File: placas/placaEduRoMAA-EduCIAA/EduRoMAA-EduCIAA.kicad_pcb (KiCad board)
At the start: 2 copper layers, 103 x 80 mm, 78 parts, among them J1 DC_IN, J2 Motor_Izq, J3 Motor_Der, J4 Bluetooth, J5 Sonar, J6 DC_OUT, J7 DC_IN, Q1 BC548, Q2 BC548, Q3 BC548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

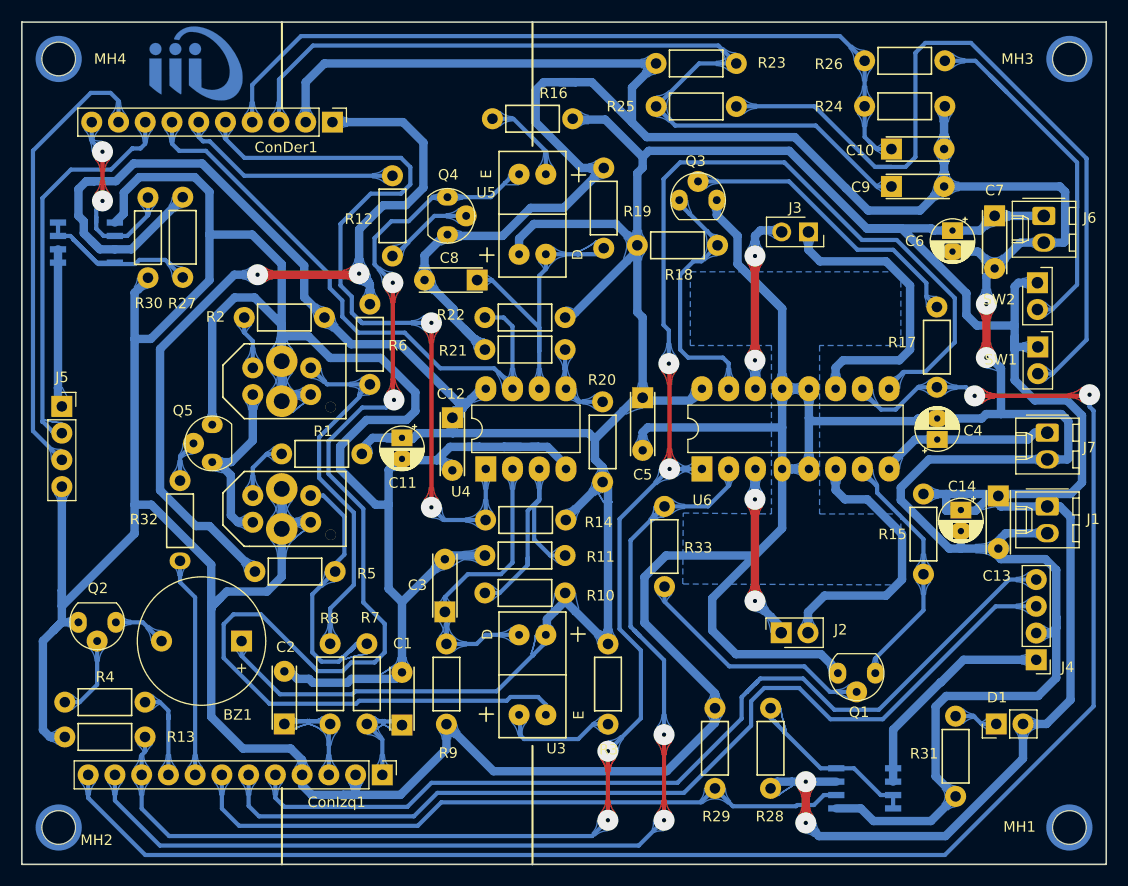
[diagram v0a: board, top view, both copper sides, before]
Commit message: [PCB] Modifico serigrafia y re-ruteo.
Modifico serigrafia y algo de ruteo
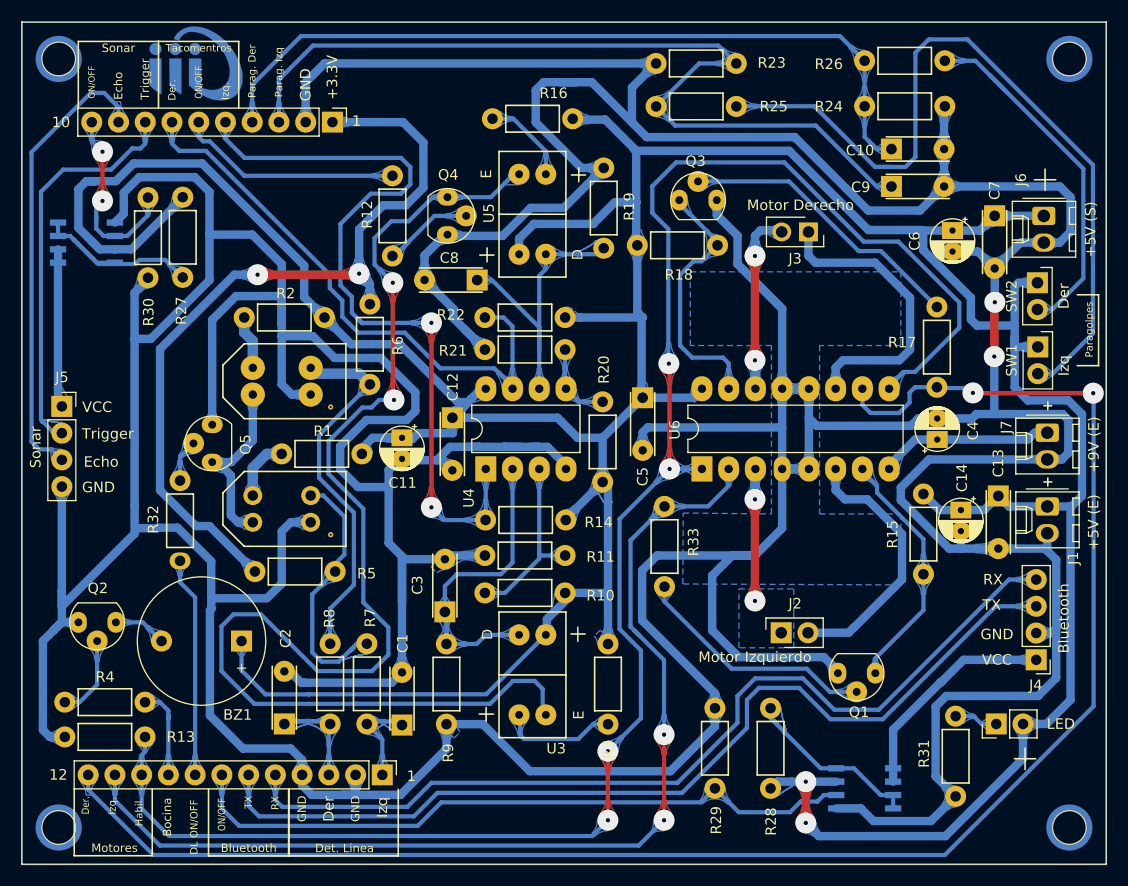
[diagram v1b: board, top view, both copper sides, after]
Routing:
- net +5V: track 416.8 -> 398.9 mm
- net GND: track 777.5 -> 766.9 mm
- net PWM_Der: track 168.8 -> 161.9 mm
- net Net-(R10-Pad2): track 23.9 -> 17.5 mm
- net GND_LED2: track 118.5 -> 122.1 mm
- net /Motor_Izq1: track 16.6 -> 13.1 mm
- net Bluetooth_Rx: track 89.2 -> 87.8 mm
- net /Motor_Izq2: track 26.5 -> 25.4 mm
- net ENABLE_Motors: track 169.4 -> 170.3 mm
- net Net-(R25-Pad2): track 75.5 -> 76.3 mm
- net Net-(Q3-Pad2): track 28.4 -> 27.6 mm
- net Net-(C3-Pad1): track 28.4 -> 29.1 mm
- net Sonar_Trig: track 37.5 -> 38.0 mm
- added copper zone on B.Cu, net /Motor_Izq1
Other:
- board text added: "+3.3V"
- board text added: "+5V (E)"
- board text added: "+5V (S)"
- board text added: "+9V (E)"
- board text added: "1"
- board text added: "10"
- board text added: "12"
- board text added: "Bluetooth"
- board text added: "Bocina"
- board text added: "DL ON/OFF"
- board text added: "Der"
- board text added: "Der."
- board text added: "Det. Linea"
- board text added: "Echo"
- board text added: "GND"
- board text added: "Habil."
- board text added: "Izq"
- board text added: "Izq."
- board text added: "LED"
- board text added: "Motor Derecho"
- board text added: "Motor Izquierdo"
- board text added: "Motores"
- board text added: "ON/OFF"
- board text added: "Parag. Der"
- board text added: "Parag. Izq"
- board text added: "Paragolpes"
- board text added: "RX"
- board text added: "Sonar"
- board text added: "TX"
- board text added: "Tacomentros"
- board text added: "Trigger"
- board text added: "VCC"

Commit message: [PCB] Revisiones de ruteado.
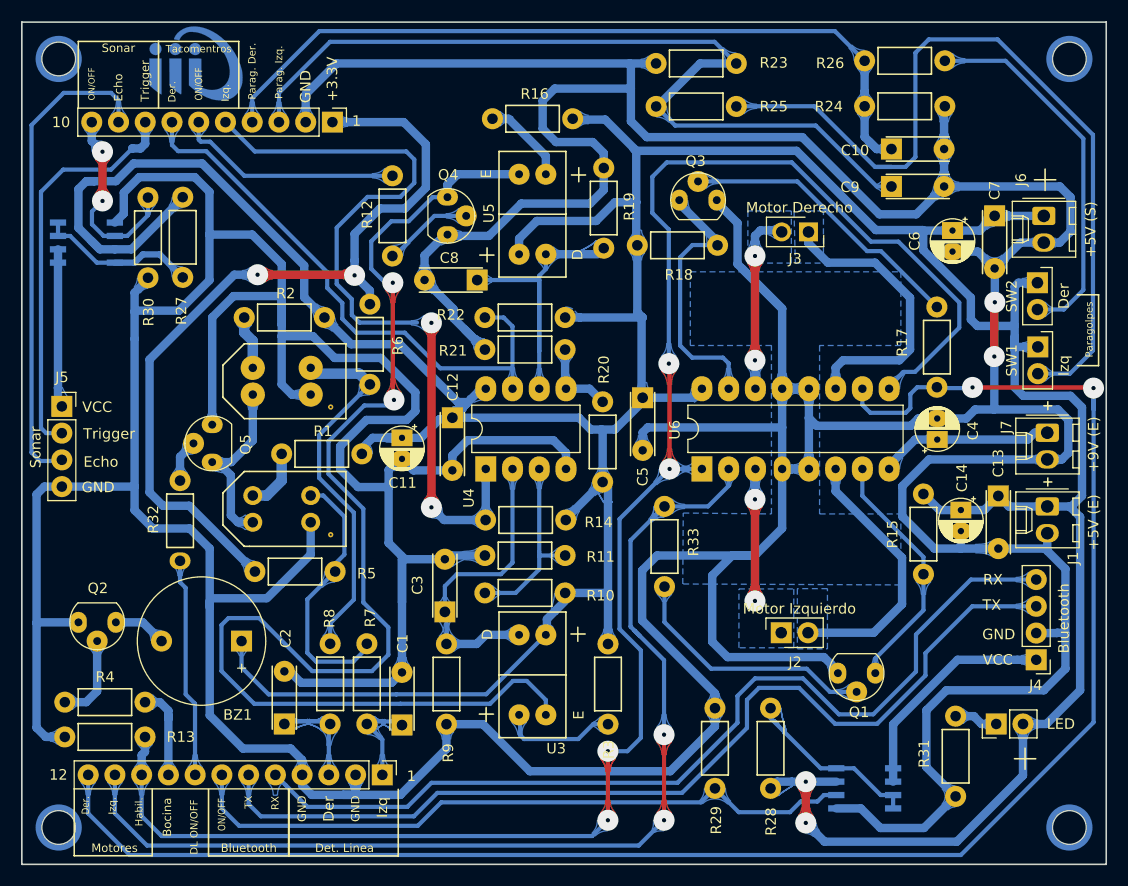
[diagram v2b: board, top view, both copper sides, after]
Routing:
- net GND: track 766.9 -> 760.6 mm
- net Net-(R27-Pad2): track 20.0 -> 15.4 mm
- net Encoder_Izq: track 78.4 -> 74.2 mm
- net PWM_Der: track 161.9 -> 165.7 mm
- net Net-(C8-Pad1): track 28.8 -> 31.4 mm
- net Net-(R25-Pad2): track 76.3 -> 78.9 mm
- net Sonar_Echo: track 43.7 -> 46.3 mm
- net ENABLE_Motors: track 170.3 -> 172.3 mm
- net Bluetooth_Tx: track 90.5 -> 92.0 mm
- net +5V: track 398.9 -> 400.3 mm
- net Net-(Q1-Pad2): track 23.2 -> 24.4 mm
- net Net-(D1-Pad1): track 5.18 -> 4.15 mm
- net Bluetooth_Rx: track 87.8 -> 88.9 mm
- net /C_2: track 25.1 -> 26.1 mm
- net Net-(R5-Pad2): track 23.7 -> 24.6 mm
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- added copper zone on B.Cu, net /Motor_Der1
- added copper zone on B.Cu, net /Motor_Der2
- added copper zone on B.Cu, net /Motor_Izq2
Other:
- board text added: "Parag. Der."
- board text added: "Parag. Izq."
- board text removed: "Parag. Der"
- board text removed: "Parag. Izq"

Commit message: [PCB] Agrego serigrafia complementaria
Agrego símbolos para serigrafia, lista para revision
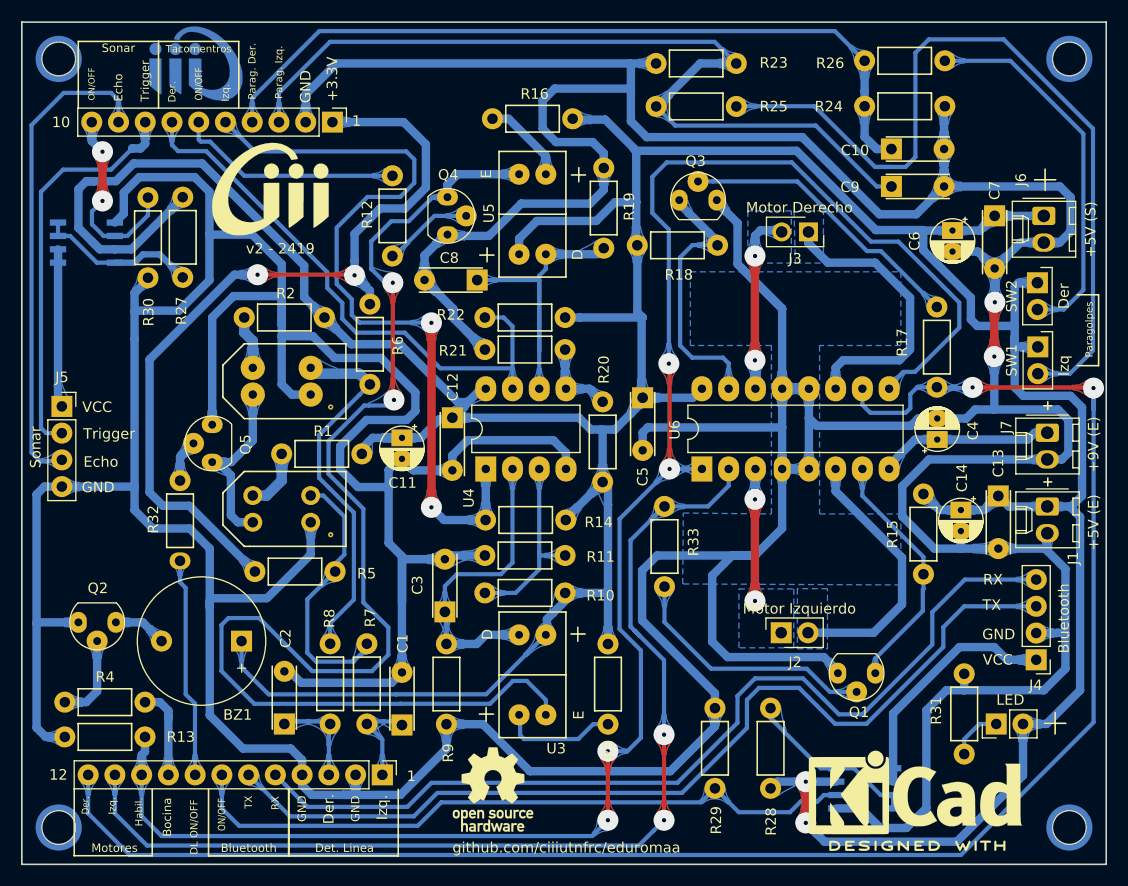
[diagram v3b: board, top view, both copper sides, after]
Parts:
- added Logo_2: Logo_CIII, lib_fp:Logo_CIII_Small_FSilk, F.Cu at (89.6, 70.9)
- added Logo_3: Logo_ohw, lib_fp:OSHW-Logo_7.5x8mm_SilkScreen, F.Cu at (110.7, 127.9)
- added Logo_4: Logo_KiCad, lib_fp:KiCad-Logo2_8mm_SilkScreen, F.Cu at (150.9, 128.1)
- moved R31 11.7 mm to (155.5, 116.9), turned to 270 degrees
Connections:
- net +3.3VA renamed +3V3
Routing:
- net /Vcc_BT: track 21.6 -> 25.0 mm
- net Bluetooth_Tx: track 92.0 -> 90.2 mm
- net GND: track 760.6 -> 758.9 mm
- net Encoder_Izq: track 74.2 -> 75.5 mm
- net Net-(D1-Pad1): track 4.15 -> 5.05 mm
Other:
- net class Default: clearance 0.5 -> 0.2
- net class power: clearance 0.5 -> 0.2
- rule trace_clearance: 0.5 -> 0.2
- board text added: "github.com/ciiiutnfrc/eduromaa"
- board text added: "v2 - 2419"

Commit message: [PCB] Arreglo teardrops
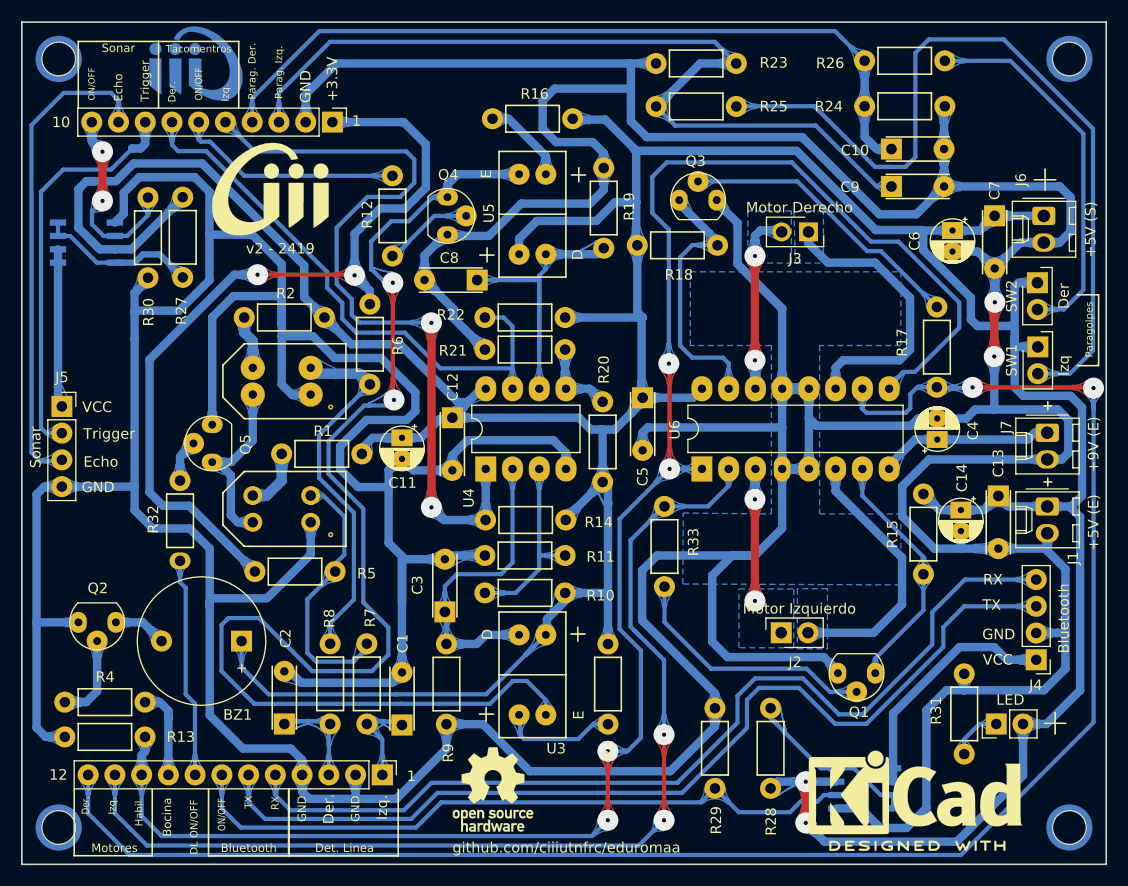
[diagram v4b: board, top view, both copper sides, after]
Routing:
- net Bluetooth_Tx: track 90.2 -> 91.9 mm
- net Bluetooth_Rx: track 88.6 -> 90.0 mm
- net GND: track 758.9 -> 757.9 mm

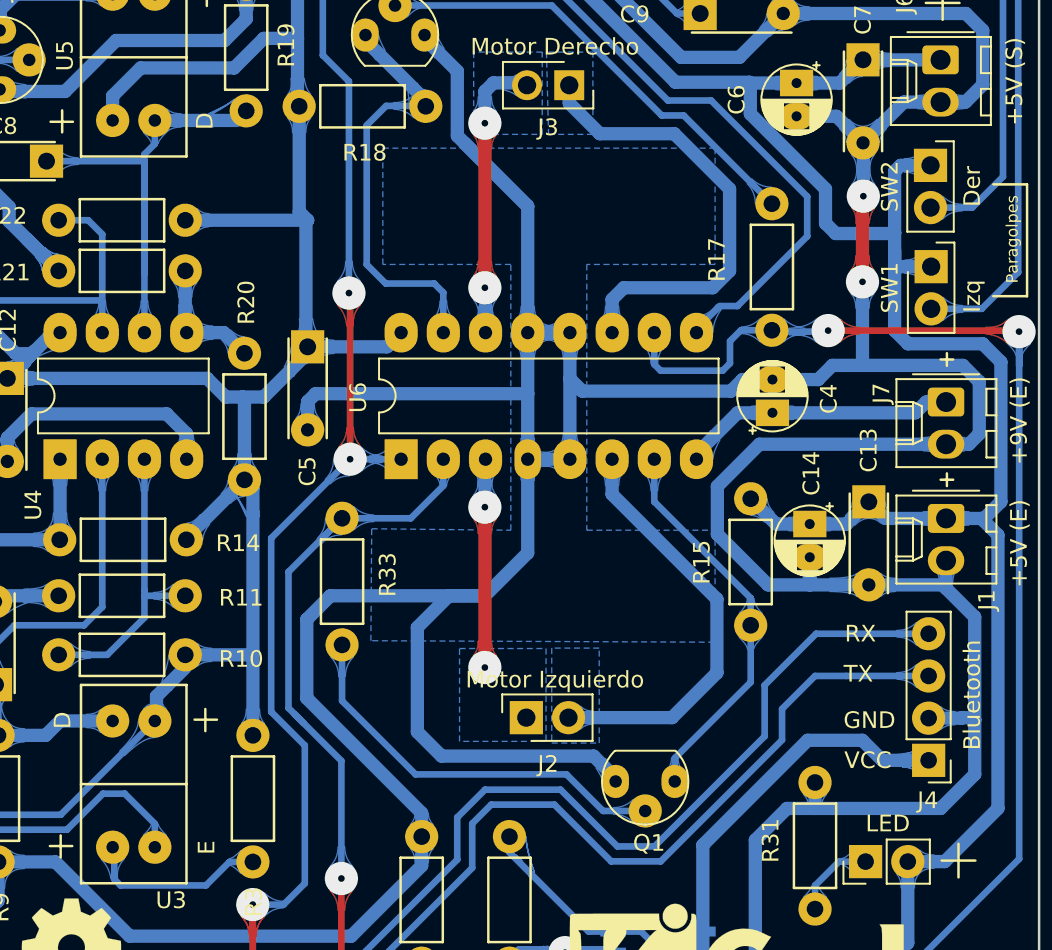
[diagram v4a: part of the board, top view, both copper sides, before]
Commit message: [PCB] Minimas modificaciones al ruteo, falta hacer un DRC
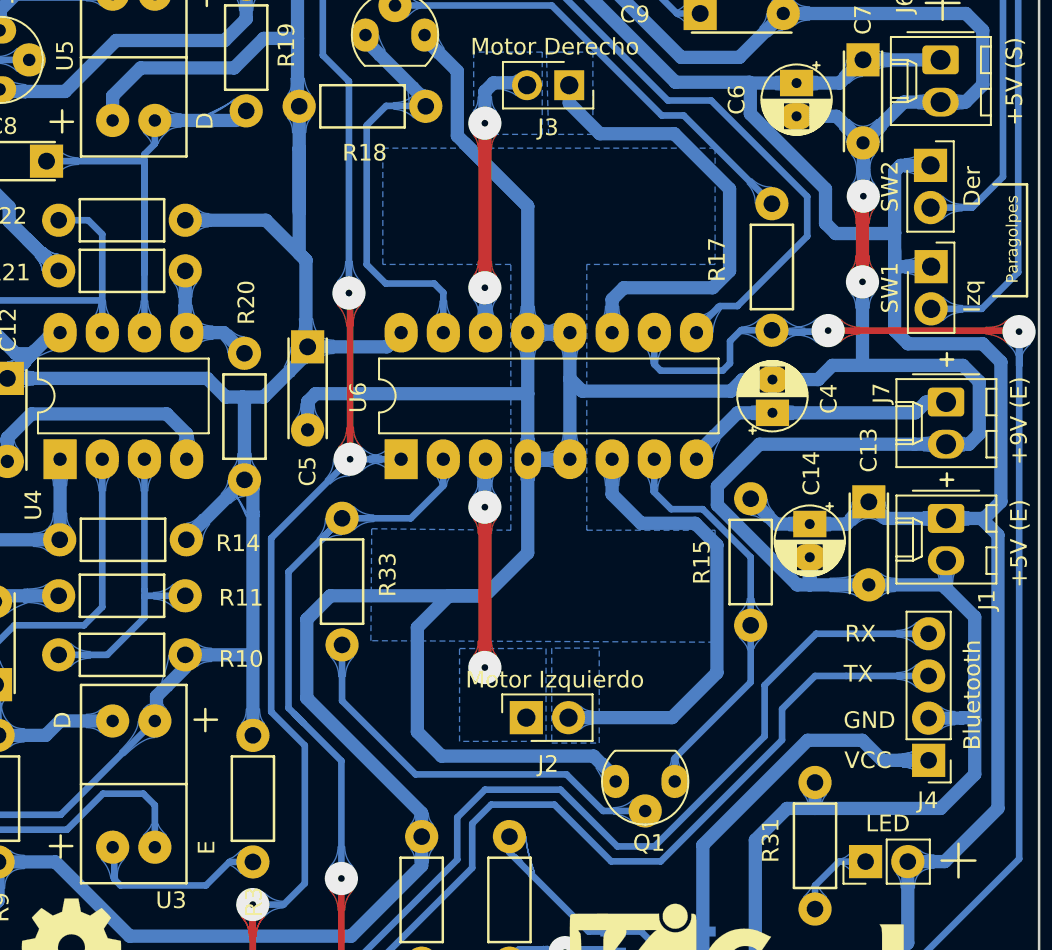
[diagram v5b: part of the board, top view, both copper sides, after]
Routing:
- net +5V: track 400.3 -> 406.4 mm
- net /Motor_Izq2: track 25.5 -> 27.4 mm
- net /C_1: track 23.7 -> 24.8 mm
- net GND: track 757.9 -> 756.9 mm
- net GND_LED2: track 122.6 -> 123.3 mm
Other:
- net class Default: clearance 0.2 -> 0.5
- net class power: clearance 0.2 -> 0.5
- rule trace_clearance: 0.2 -> 0.5
